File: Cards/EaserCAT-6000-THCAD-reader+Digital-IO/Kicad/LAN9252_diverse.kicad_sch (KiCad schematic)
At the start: 29 parts, among them CN1 10pF, CN2 10pF, J11 5V input, U2 AT24CS32-SSHM, U9 AMS1117-3.3

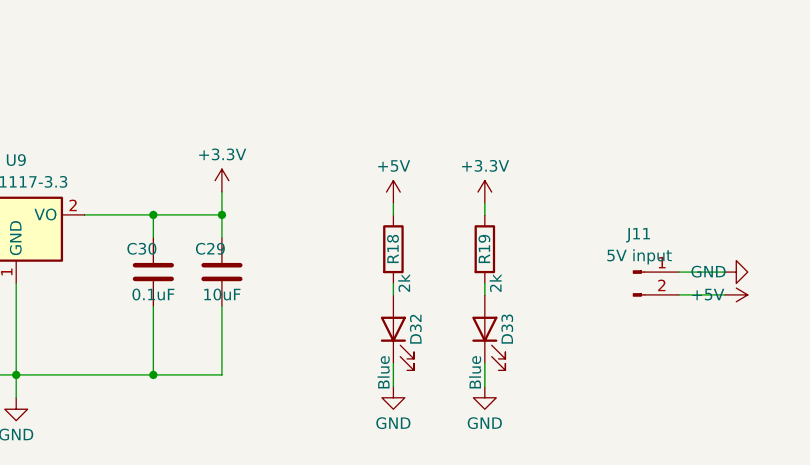
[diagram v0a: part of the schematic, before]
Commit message: Modified, switch marker postions for C28 and R17
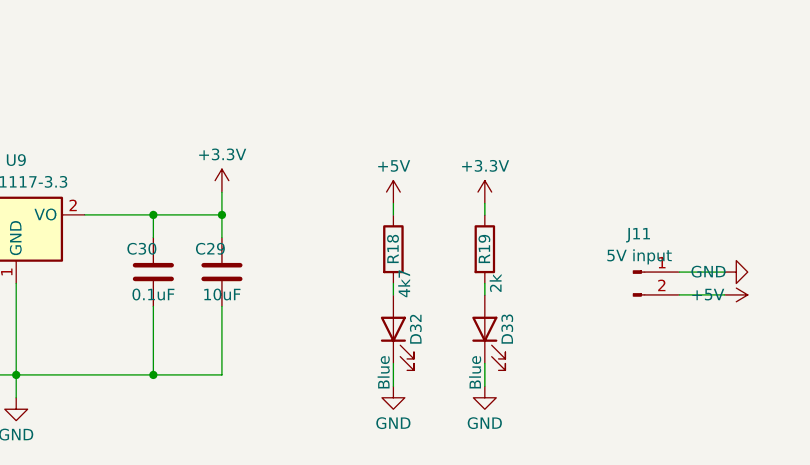
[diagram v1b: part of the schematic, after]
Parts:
- R18: value 2k -> 4k7
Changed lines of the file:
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@@
 			)
 		)
-		(property "Value" "2k"
+		(property "Value" "4k7"
 			(at 95.25 163.83 90)
 			(effects
